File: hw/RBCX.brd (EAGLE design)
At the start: 100 x 100 mm, 464 parts, among them IC1 AMS1117-3.3, IC10 INA180A4, IC11 INA180A4, IC12 MPU-6050, IC13 STM32F103VCT6, IC2 DRV8833PWP, IC3 INA180A4, IC4 INA180A4, IC5 DRV8833PWP, IC6 INA180A4, IC7 INA180A4, IC8 INA180A4, IC9 INA180A4, P1 M1, P2 M2, P3 M3, P4 M4, Q1 NCE20P45Q, Q10 2N7002, Q2 NCE20P45Q, Q3 2N7002, Q4 2N7002, Q5 2N7002, Q6 2N7002, Q7 2N7002, Q8 2N7002, Q9 2N7002, X1 POWER_IN, X2 POWER_OUT, X3 52559-3092, X4 uUSB, Y1 5032/2P, Y2 3215_2P

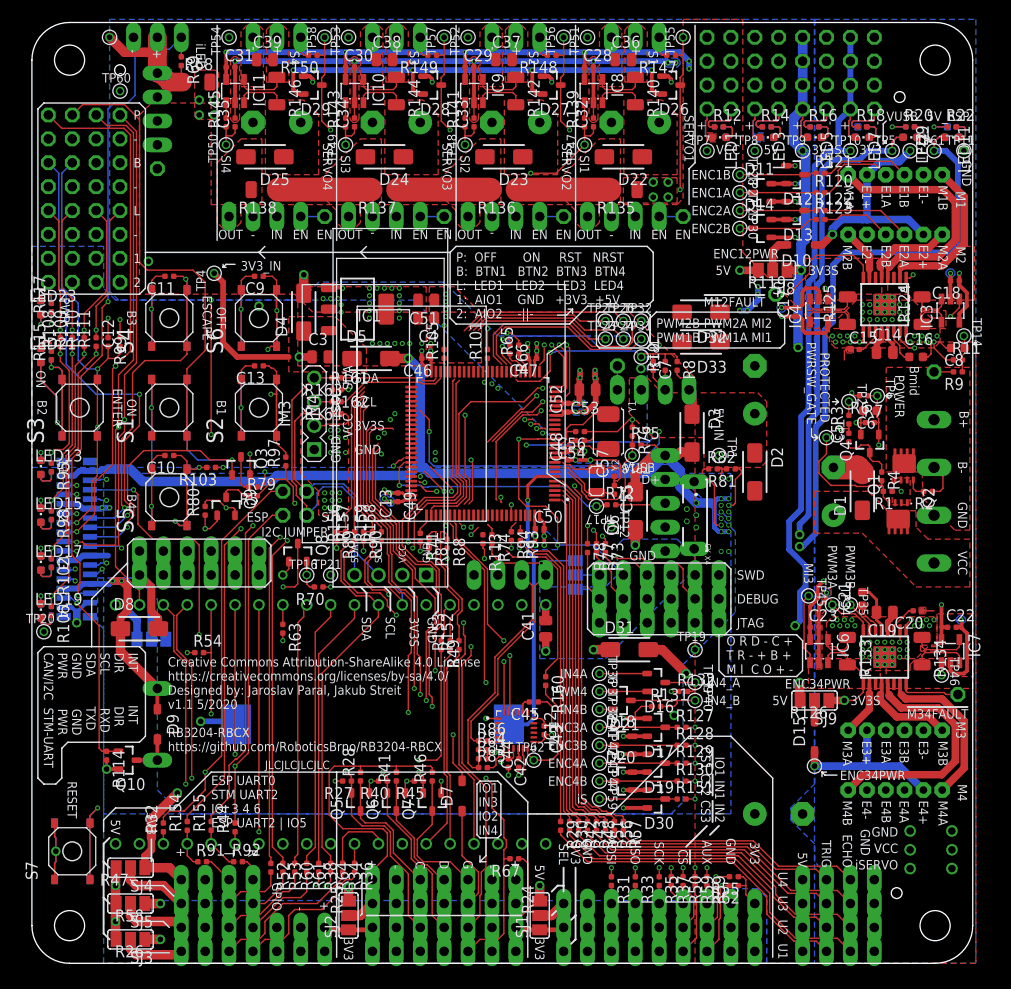
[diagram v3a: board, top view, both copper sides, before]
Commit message: hw: add middle battery voltage (with overvoltage protection) to the power input terminal block (replaced by 3-pin)
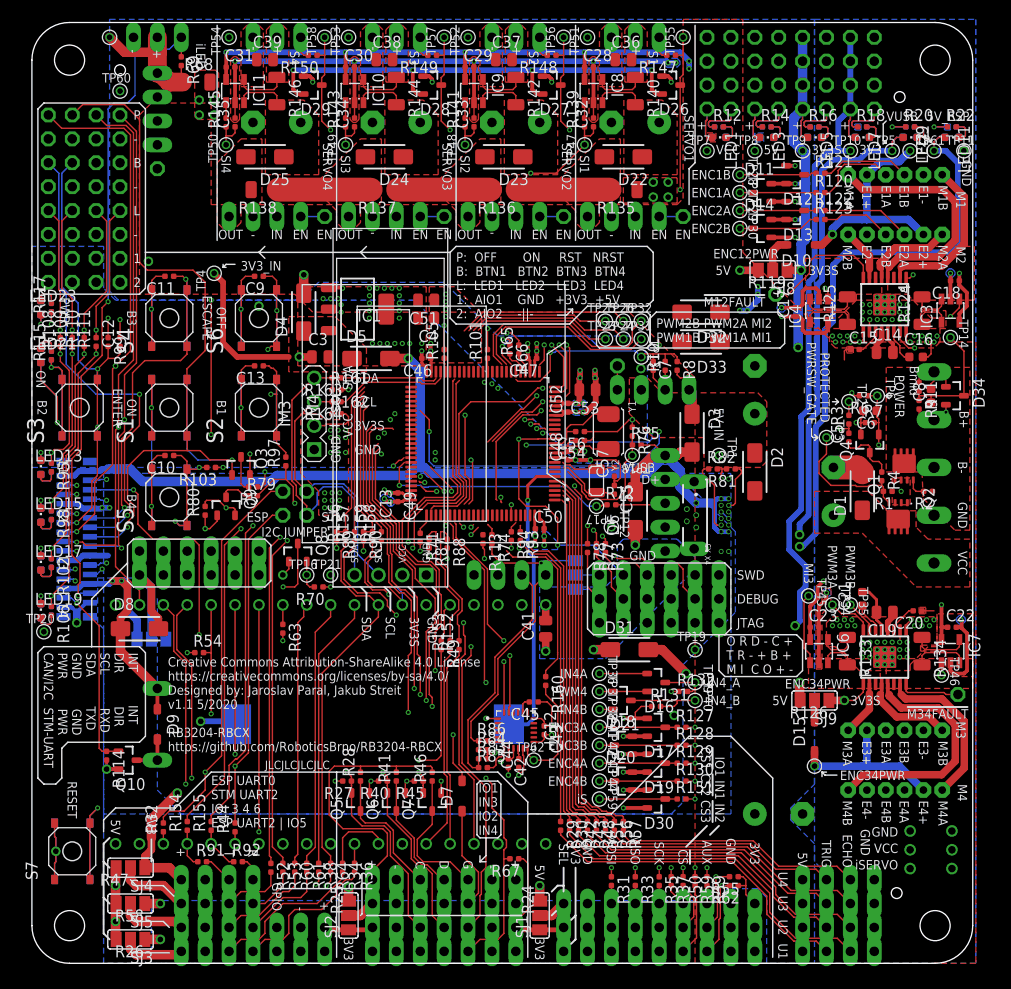
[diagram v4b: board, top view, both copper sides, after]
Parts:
- removed JP4: VBAT/2, pinhead:1X01
- added D34: BAS40-04, diode:SOT23
- X1: device con-wago-508:W237-132 -> con-wago-508:W237-133
- moved C8 5.83 mm to (95.6, 60.3), turned to 90 degrees
- moved R9 5.41 mm to (94.3, 59.4), turned to 270 degrees
- moved R11 5.02 mm to (94.3, 61.3), turned to 270 degrees
- moved X1 2.54 mm to (95.2, 57.8)
- moved TP14 1.44 mm to (97.6, 66.5)
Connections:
- removed net VBAT/2: JP4.1, R9.2
- new net BAT_MID: R9.2, X1.2
- net +3V3S: now also D34.2
- net BAT+: now also X1.3; no longer X1.1
- net GND: now also D34.1, X1.1; no longer X1.2
- net V_BAT/2: now also D34.3
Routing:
- net +3V3S: track 539.3 -> 551.0 mm, vias 97 -> 98
- net V_BAT/2: track 58.5 -> 66.3 mm
- net BAT_MID: track 0.00 -> 2.43 mm
- net GND: track 630.1 -> 627.8 mm
- net VBAT/2: track 2.07 -> 0.00 mm

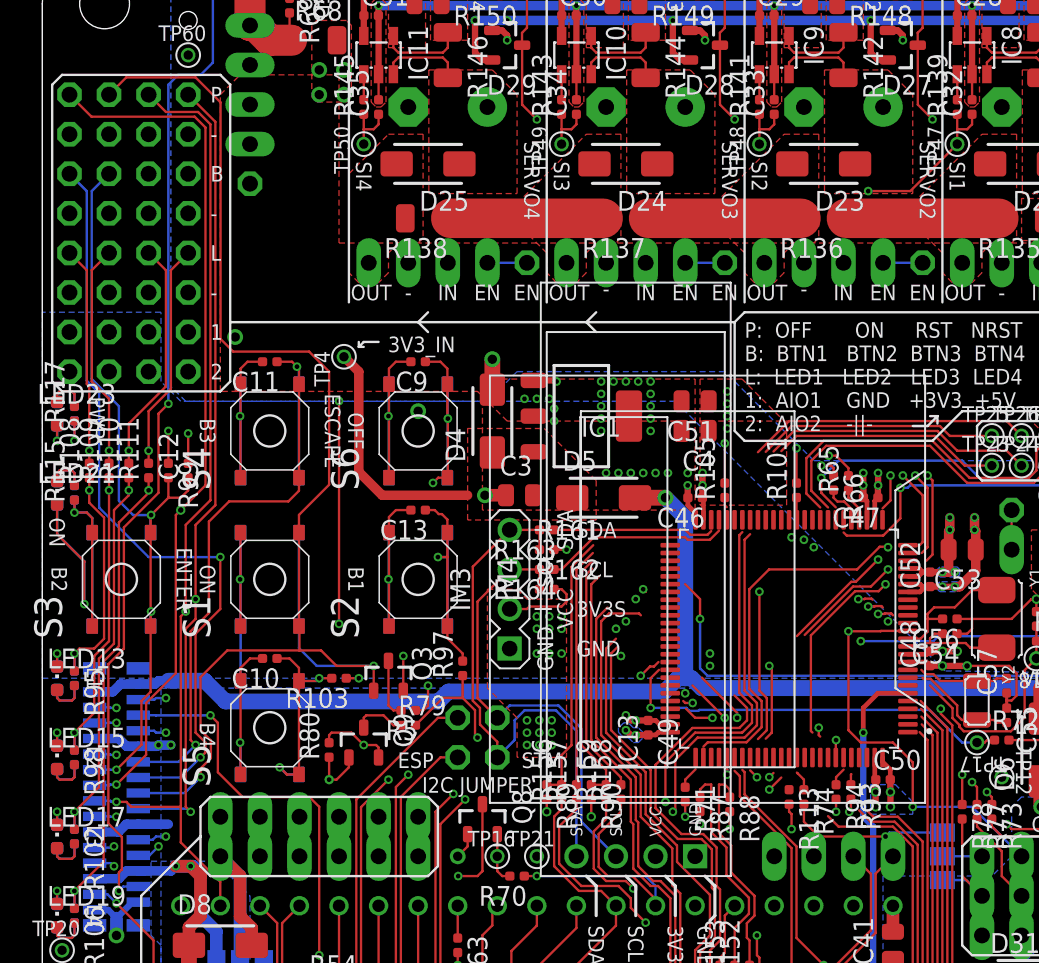
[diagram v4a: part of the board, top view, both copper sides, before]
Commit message: hw: fix schematic related issues
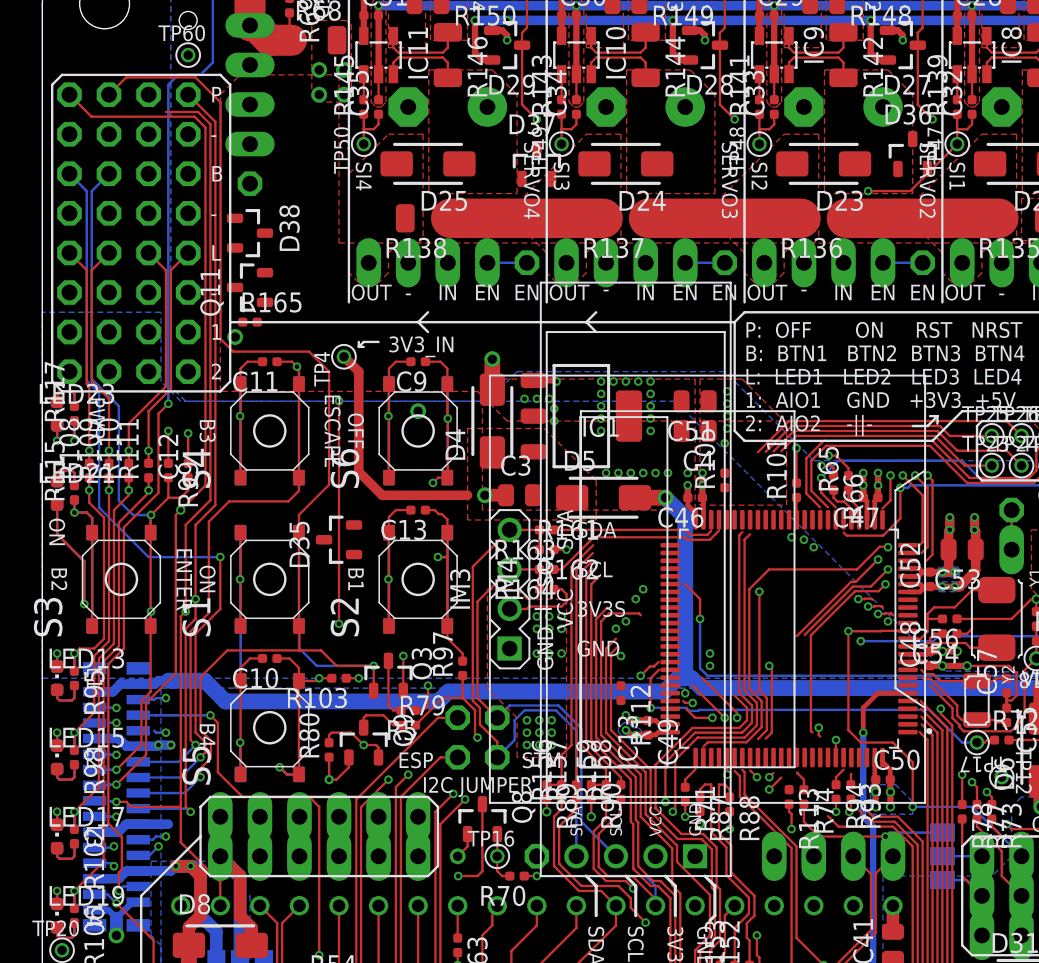
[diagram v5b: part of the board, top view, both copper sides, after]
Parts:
- removed TP21: (no value), test_points:TP_06
- added D35: BAS40-04, diode:SOT23
- added D36, D37, D38: BAS40-05, diode:SOT23
- added JP4: BUZZER, pinhead:1X01
- added Q11: 2N7002, transistors:SOT23
- added R112, R165: 4k7, rcl_upravena:R0402
- JP1: value IM1_EN -> 3V3_EN
- JP29: value IM9_EN -> ILED_EN
- R105: value 330R -> 2k2
- R114: value 100k -> 1M
- moved R105 0.64 mm to (43.8, 65.4)
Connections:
- removed net IM7_EN: IM1.EN, JP1.1
- removed net IM9_EN: IM2.EN, JP29.1
- new net 3V3_EN: D38.2, IM1.EN, JP1.1
- new net ESP-EN: JP44.5, Q11.3, R165.1, X3.15
- new net ILED_EN: D38.1, IM2.EN, JP29.1
- net +3V3S: now also D35.2, D36.3, D37.3, D38.3, Q11.1, R112.2, R165.2; no longer Q8.1
- net BUTTON_OFF: now also D35.3
- net BUZZER-GATE: now also JP4.1; no longer TP21.P$1
- net ESP-I2C-SCL: no longer X3.25
- net ESP-I2C-SDA: no longer X3.24
- net ESP_EN: now also Q11.2, Q8.1, R112.1; no longer JP44.5, X3.15
- net GND: now also D35.1
- net SERVO1_EN: now also D36.2
- net SERVO2_EN: now also D36.1
- net SERVO3_EN: now also D37.2
- net SERVO4_EN: now also D37.1
- net STM-I2C-SCL: now also X3.25
- net STM-I2C-SDA: now also X3.24
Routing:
- net ESP_EN: track 138.2 -> 133.7 mm, vias 4 -> 5
- net BUZZER-GATE: track 67.2 -> 62.9 mm
- net BUTTON-OFF: track 109.9 -> 107.3 mm
- net IM9_EN: track 2.54 -> 0.00 mm
- net ILED_EN: track 0.00 -> 2.54 mm
- net IM7_EN: track 2.54 -> 0.00 mm
- net 3V3_EN: track 0.00 -> 2.54 mm
- net +3V3S: track 551.0 -> 549.3 mm, vias 98 -> 97
- net ESP-I2C-SDA: track 94.9 -> 93.9 mm
- net ESP-I2C-SCL: track 104.5 -> 103.6 mm
- net BUTTON_OFF: track 0.67 -> 0.00 mm

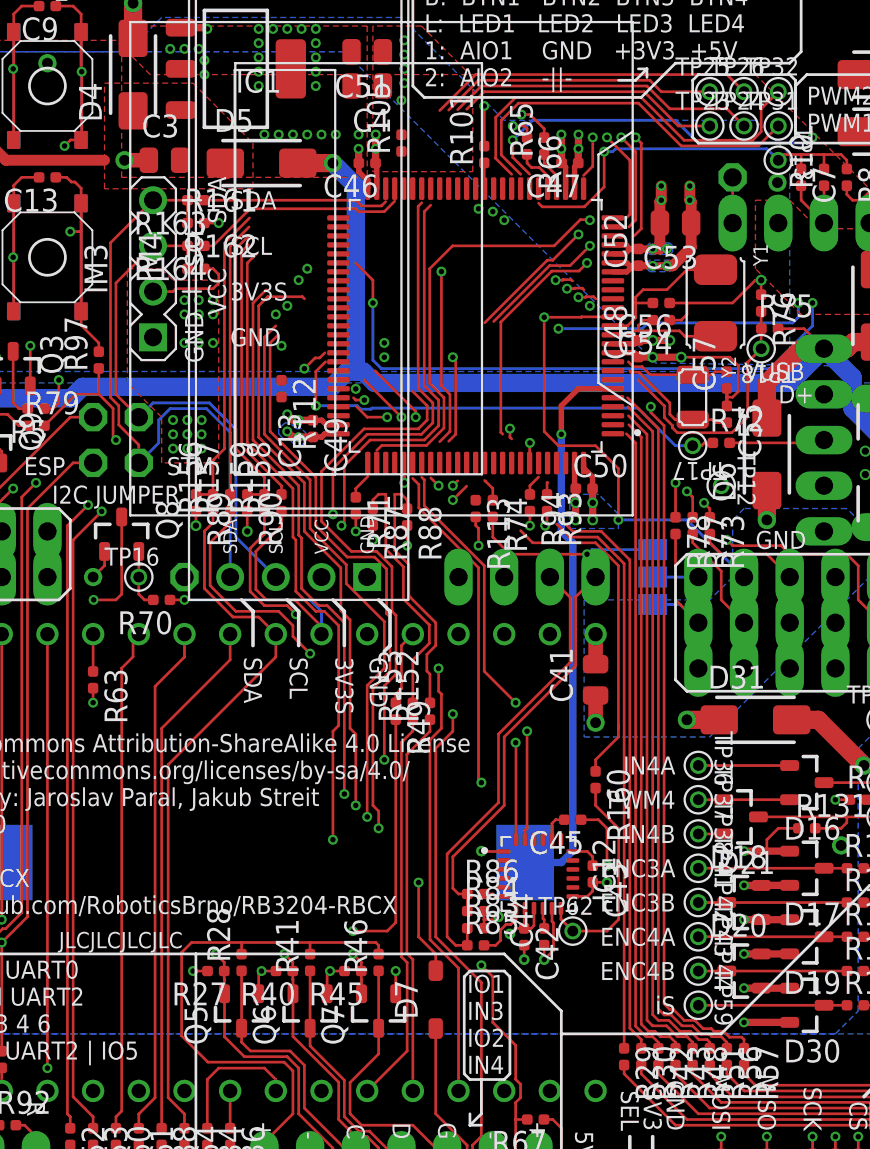
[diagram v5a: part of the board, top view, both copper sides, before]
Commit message: hw: swap button 3 and 4, routing
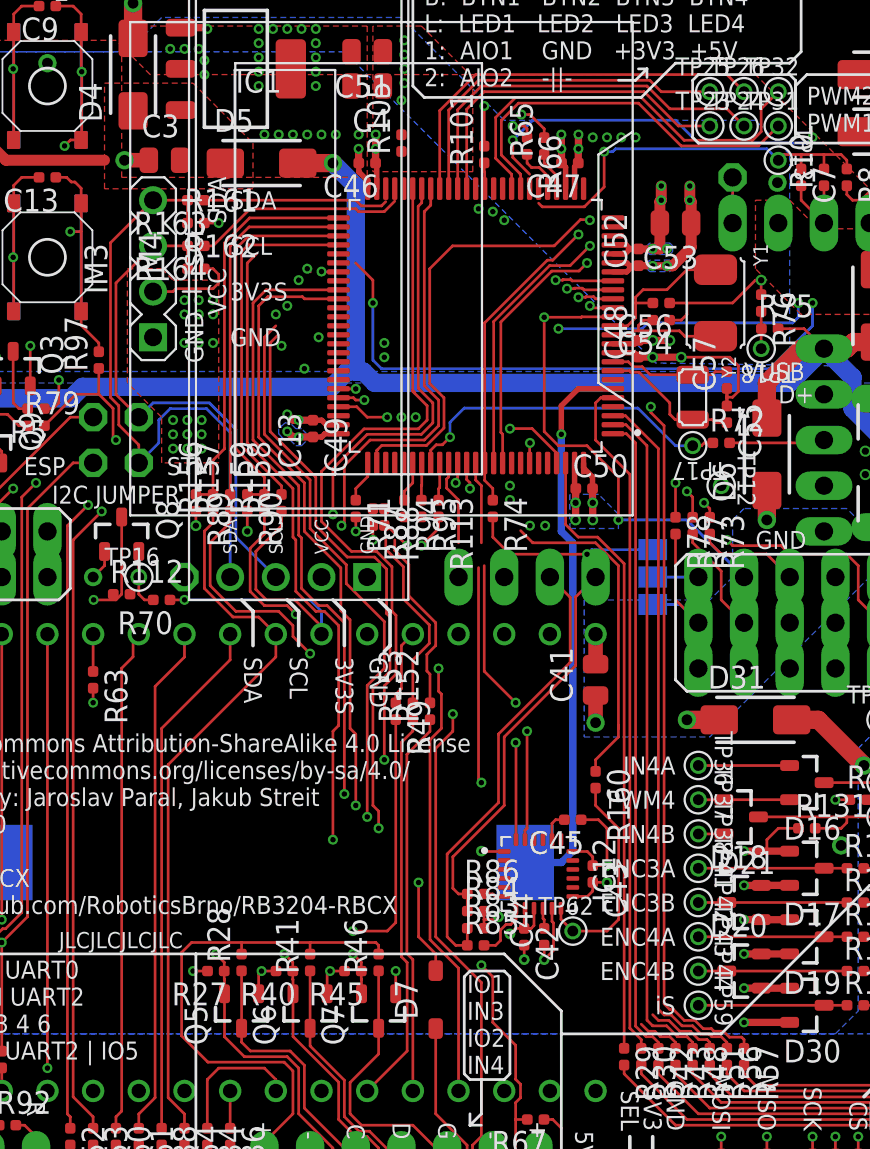
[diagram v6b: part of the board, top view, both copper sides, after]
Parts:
- moved R112 14.5 mm to (28.3, 40.3), turned to 0 degrees
- moved R93 6.99 mm to (44.9, 45.1)
- moved R94 6.99 mm to (44.0, 45.1)
- moved R113 2.06 mm to (45.9, 45.1)
- moved R88 1.27 mm to (42.9, 44.6)
- moved R71 0.16 mm to (41.3, 45.1)
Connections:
- net EXPANDER-COM-DIR renamed CONTROL-DIR
- net EXPANDER-COM-INT renamed CONTROL-INT
- net EXPANDER-UART-RX renamed CONTROL-RX/SDA
- net EXPANDER-UART-TX renamed CONTROL-TX/SCL
- net STM-CAN-RX/I2C-SCL renamed STM-CAN-RX
- net STM-CAN-TX/I2C-SDA renamed STM-CAN-TX
- removed net CONTROL_RX: IC13.48
- removed net CONTROL_TX: IC13.47
- removed net ESP_COM_RX: R152.2, R88.1
- removed net ESP_COM_TX: R153.2, R87.1
- new net CONTROL_RX/SDA: IC13.48, R152.2, R88.1
- new net CONTROL_TX/SCL: IC13.47, R153.2, R87.1
- net BUTTON2: now also IC13.57; no longer IC13.37
- net BUTTON3: now also IC13.37; no longer IC13.57
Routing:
- net UTS3_ECHO: track 38.5 -> 4.14 mm
- net UTS2_ECHO: track 36.3 -> 7.22 mm
- net ESP_EN: track 133.7 -> 109.1 mm
- net BUTTON2: track 54.2 -> 38.7 mm
- net ESP_COM_TX: track 14.3 -> 0.00 mm
- net ESP_COM_RX: track 14.1 -> 0.00 mm
- net BUTTON4: track 33.6 -> 20.5 mm
- net VUSB_DET: track 14.3 -> 2.09 mm
- net PWM4: track 51.3 -> 62.7 mm
- net CONTROL_TX/SCL: track 0.00 -> 10.4 mm
- net CONTROL_RX/SDA: track 0.00 -> 10.3 mm
- net ENC1B/SWO: track 55.3 -> 64.0 mm
- net ENC2A: track 51.8 -> 59.7 mm
- net USB_DP_PULLUP: track 25.8 -> 18.8 mm
- net IN4B: track 33.2 -> 26.7 mm
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
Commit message: hw: routing
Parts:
- removed Q11: 2N7002, transistors:SOT23
- removed R165: 4k7, rcl_upravena:R0402
- D35: value BAS40-04 -> BAS40-05
- R112: value 4k7 -> 1M
- moved R112 29.9 mm to (10.2, 16.5)
- moved R105 24.0 mm to (20.5, 70.8), turned to 0 degrees
- moved TP62 21.6 mm to (44.5, 41.3)
- moved R79 16.4 mm to (7.30, 46.8)
- moved R163 15.3 mm to (29.8, 47.1)
- moved TP4 14.4 mm to (27.6, 61.6)
- moved Q9 13.9 mm to (7.30, 44.6)
- moved R80 13.6 mm to (6.35, 41.9), turned to 270 degrees
- moved R161 13.1 mm to (29.8, 48.1)
- moved R164 9.40 mm to (29.8, 50.6)
- moved R162 9.09 mm to (29.8, 49.7)
- moved R160 8.90 mm to (52.9, 21.3), turned to 90 degrees
- moved D35 7.01 mm to (19.7, 68.6), turned to 180 degrees
- moved R87 4.52 mm to (37.8, 45.4)
- moved R152 4.45 mm to (41.0, 33.8)
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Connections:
- net ENC1B-SWO renamed ENC3B-SWO
- removed net ENC1B/SWO: D12.3, IC13.89, R121.1, R74.1, TP28.P$1
- removed net ENC3B: D18.3, IC13.60, R128.1, TP42.P$1
- removed net ESP-EN: JP44.5, Q11.3, R165.1, X3.15
- new net ENC1B: D12.3, IC13.60, R121.1, TP28.P$1
- new net ENC3B/SWO: D18.3, IC13.89, R128.1, R74.1, TP42.P$1
- net +3V3S: now also D35.3; no longer D35.2, Q11.1, R165.2
- net BUTTON-3: now also R79.2
- net BUTTON1: no longer R79.2
- net BUTTON_OFF: now also D35.1; no longer D35.3
- net ENC1A: now also IC13.59; no longer IC13.77
- net ENC2A: now also IC13.23; no longer IC13.90
- net ENC2B: now also IC13.24; no longer IC13.91
- net ENC3A: now also IC13.77; no longer IC13.59
- net ENC4A: now also IC13.90; no longer IC13.23
- net ENC4B: now also IC13.91; no longer IC13.24
- net ESP_EN: now also D35.2, JP44.5, X3.15; no longer Q11.2
- net GND: no longer D35.1
- net MPU-INT: no longer TP62.P$1
- net MPU_INT: now also TP62.P$1
- net SI1: now also IC13.18; no longer IC13.15
- net SI2: now also IC13.17; no longer IC13.16
- net SI3: now also IC13.16; no longer IC13.17
- net SI4: now also IC13.15; no longer IC13.18
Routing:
- net GND: track 627.8 -> 537.3 mm, vias 142 -> 143
- net ESP_EN: track 109.1 -> 176.3 mm, vias 5 -> 7
- net ENC3B: track 64.3 -> 0.00 mm, vias 1 -> 0
- net ENC1B/SWO: track 64.0 -> 0.00 mm, vias 1 -> 0
- net ENC1B: track 0.00 -> 63.5 mm, vias 0 -> 1
- net 3V3_EN: track 2.54 -> 64.5 mm, vias 0 -> 1
- net UTS3_ECHO: track 4.14 -> 59.4 mm, vias 0 -> 2
- net ENC3B/SWO: track 0.00 -> 45.3 mm, vias 0 -> 1
- net UTS2_ECHO: track 7.22 -> 45.2 mm, vias 0 -> 2
- net BUTTON_OFF: track 0.00 -> 33.1 mm, vias 0 -> 2
- net MPU_INT: track 18.2 -> 50.5 mm, vias 0 -> 2
- net SERVO1: track 44.1 -> 70.5 mm
- net SERVO2: track 34.9 -> 59.5 mm
- net CONTROL_TX/SCL: track 10.4 -> 34.9 mm, vias 0 -> 2
- net STM-I2C-SCL: track 56.9 -> 81.4 mm, vias 1 -> 2
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
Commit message: hw: routed
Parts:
- moved D33 21.8 mm to (92.2, 60.5), turned to 90 degrees
- moved D32 18.0 mm to (84.7, 57.3), turned to 270 degrees
- moved TP1 9.38 mm to (64.8, 58.4)
- moved TP3 6.87 mm to (88.3, 61.6)
- moved D3 3.50 mm to (72.9, 58.6)
- moved X4 3.42 mm to (67.3, 48.9)
- moved JP33 3.17 mm to (70.5, 48.9)
- moved R81 1.77 mm to (74.6, 54.3), turned to 90 degrees
- moved R82 1.77 mm to (72.7, 54.3), turned to 90 degrees
- moved X5 1.27 mm to (73.7, 48.9)
- moved R8 0.95 mm to (67.6, 63.5)
- moved R10 0.64 mm to (66.7, 63.5)
- moved R2 0.48 mm to (94.8, 50.2)
- moved C7 0.32 mm to (65.7, 63.5)
- moved C16 0.22 mm to (93.8, 64.6)
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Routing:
- net 5V_IN: track 0.00 -> 19.1 mm
- net PWRSW_GATE: track 14.1 -> 31.8 mm, vias 0 -> 1
- net VUSB: track 164.7 -> 170.7 mm, vias 2 -> 5
- net BAT+_PROTECTED: track 13.3 -> 18.8 mm, vias 1 -> 2
- net GND: track 537.3 -> 542.8 mm
- net +5V: track 62.5 -> 65.4 mm, vias 18 -> 19
- net USB_ID: track 2.56 -> 4.83 mm
- net +3V3S: track 565.8 -> 567.9 mm
- net ESP_+5V: track 85.7 -> 86.9 mm
- net USB_CC1: track 7.61 -> 6.61 mm
- net V_BAT: track 20.9 -> 20.0 mm
- net +3V3: track 134.6 -> 135.3 mm
- net BUTTON-ON: track 155.9 -> 156.7 mm
- net USB_CC2: track 5.27 -> 4.53 mm
- net USB_DM: track 73.6 -> 72.9 mm
- added copper zone on layer 16, net VUSB
- removed copper zone on layer 1, net 5V_IN
